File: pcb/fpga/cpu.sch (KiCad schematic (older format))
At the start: 53 parts, among them CON1 USB-MINI-B, P1 BANK1, P2 BANK2, P3 CONN_6, P4 BANK3, P5 BANK4, P6 PWR, U1 EPCS1, U2 EP1C3T100, U3 BA15BC0FP-E2_-_LDO, U4 LM1084IS-3.3/NOPB

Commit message: Latest pcb
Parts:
- removed C13, C6: 0.01uF, symbol Csmall
- removed U3: BA15BC0FP-E2_-_LDO, TO-252, symbol BA15BC0FP-E2_-_LDO
- added U2: LMS1585/7, TO-263, symbol LMS1585/7
- C1, C14, C15, C16, C17, C18: footprint (none) -> Capacitors_SMD:C_0805_HandSoldering
- C10: renamed from C7; footprint (none) -> Capacitors_SMD:C_0805_HandSoldering
- C11: renamed from C8; footprint (none) -> Capacitors_SMD:C_0805_HandSoldering
- C12: renamed from C9; footprint (none) -> Capacitors_SMD:C_0805_HandSoldering
- C13: renamed from C11; footprint (none) -> Capacitors_SMD:C_0805_HandSoldering
- C19: renamed from C23; footprint (none) -> Capacitors_SMD:c_elec_4x5.3
- C2: renamed from C3; footprint (none) -> Capacitors_SMD:C_0805_HandSoldering
- C20: renamed from C25; footprint (none) -> Capacitors_SMD:c_elec_4x5.3
- C21: renamed from C27; footprint (none) -> Capacitors_SMD:c_elec_4x5.3
- C22: renamed from C19; footprint (none) -> Capacitors_SMD:c_elec_4x5.3
- C23: renamed from C20; footprint (none) -> Capacitors_SMD:C_0805
- C24: renamed from C21; footprint (none) -> Capacitors_SMD:C_0805
- C25: renamed from C2; footprint (none) -> Capacitors_SMD:C_0805
- C3: renamed from C5; footprint (none) -> Capacitors_SMD:C_0805_HandSoldering
- C4: renamed from C10; footprint (none) -> Capacitors_SMD:C_0805_HandSoldering
- C5: renamed from C12; footprint (none) -> Capacitors_SMD:C_0805_HandSoldering
- C6: renamed from C22; footprint (none) -> Capacitors_SMD:c_elec_4x4.5
- C7: renamed from C24; footprint (none) -> Capacitors_SMD:c_elec_4x4.5
- C8: renamed from C26; footprint (none) -> Capacitors_SMD:c_elec_4x4.5
- C9: renamed from C4; footprint (none) -> Capacitors_SMD:C_0805_HandSoldering
- CON1: footprint (none) -> Connect:USB_Mini-B
- D1, D2, D3, D4, D5, D6, D7, D8: footprint (none) -> LEDs:LED-0805
- FB1: renamed from FB2; footprint (none) -> Resistors_SMD:R_2816_HandSoldering
- FB2: renamed from FB1; footprint (none) -> Resistors_SMD:R_2816_HandSoldering
- OSC1: value 501AAA -> Si501AAA
- P1: renamed from P6; footprint (none) -> Pin_Headers:Pin_Header_Straight_1x02
- P2: renamed from P4; footprint (none) -> Pin_Headers:Pin_Header_Straight_2x08
- P3: renamed from P1; footprint (none) -> Pin_Headers:Pin_Header_Straight_2x06
- P4: renamed from P2; footprint (none) -> Pin_Headers:Pin_Header_Straight_2x09
- P5: footprint (none) -> Pin_Headers:Pin_Header_Straight_2x09
- P6: renamed from P3; footprint (none) -> Pin_Headers:Pin_Header_Straight_1x06
- R1: renamed from R2; footprint (none) -> Resistors_SMD:R_0805_HandSoldering
- R2: renamed from R1; footprint (none) -> Resistors_SMD:R_0805_HandSoldering
- RP1: footprint (none) -> Resistors_SMD:R_Array_Convex_4x1206
- RP2: footprint (none) -> Resistors_SMD:R_Array_Convex_8x0602
- U1: footprint (none) -> SMD_Packages:SOIC-8-N
- U3: renamed from U4; footprint TO-263 -> SMD_Packages:TO-263
- U4: renamed from U2; footprint (none) -> Housings_QFP:TQFP-100_14x14mm_Pitch0.5mm
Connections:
- net +1.5V: now also U2.2 (OUT); no longer C1.1, C13.1, C14.1, C15.1, C16.1, C17.1, C18.1, C20.1, C21.1, C22.1, C23.1, C24.1, C25.1, C4.1, C5.1, FB2.2, OSC1.4 (VDD), P1.1 (P1), P6.6, RP1.1 (P1), RP1.2 (P2), RP1.3 (P3), RP1.4 (P4), U1.3 (Vcc), U1.7 (Vcc), U1.8 (Vcc), U3.2 (OUT), U4.18 (VCCIO1), U4.31 (VCCIO4), U4.46 (VCCIO4), U4.59 (VCCIO3), U4.80 (VCCIO2), U4.9 (VCCA_PLL1), U4.95 (VCCIO2)
- net GND: no longer C6.2, C7.2, C8.2
- net at C19.1, C6.1, FB1.2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: now also U2.3 (IN)
- net 3V3 renamed +3.3V
- net +3.3V: now also C1.1, C13.1, C14.1, C15.1, C16.1, C17.1, C18.1, C20.1, C21.1, C25.1, C4.1, C5.1, OSC1.4 (VDD), P1.1 (P1), P6.6, RP1.1 (P1), RP1.2 (P2), RP1.3 (P3), RP1.4 (P4), U1.3 (Vcc), U1.7 (Vcc), U1.8 (Vcc), U3.2 (OUT), U4.18 (VCCIO1), U4.31 (VCCIO4), U4.46 (VCCIO4), U4.59 (VCCIO3), U4.80 (VCCIO2), U4.95 (VCCIO2)
- new net: C6.2, C7.2, C8.2, U2.1 (GND)
- new net VPLL: C22.1, C23.1, C24.1, FB2.2, U4.9 (VCCA_PLL1)

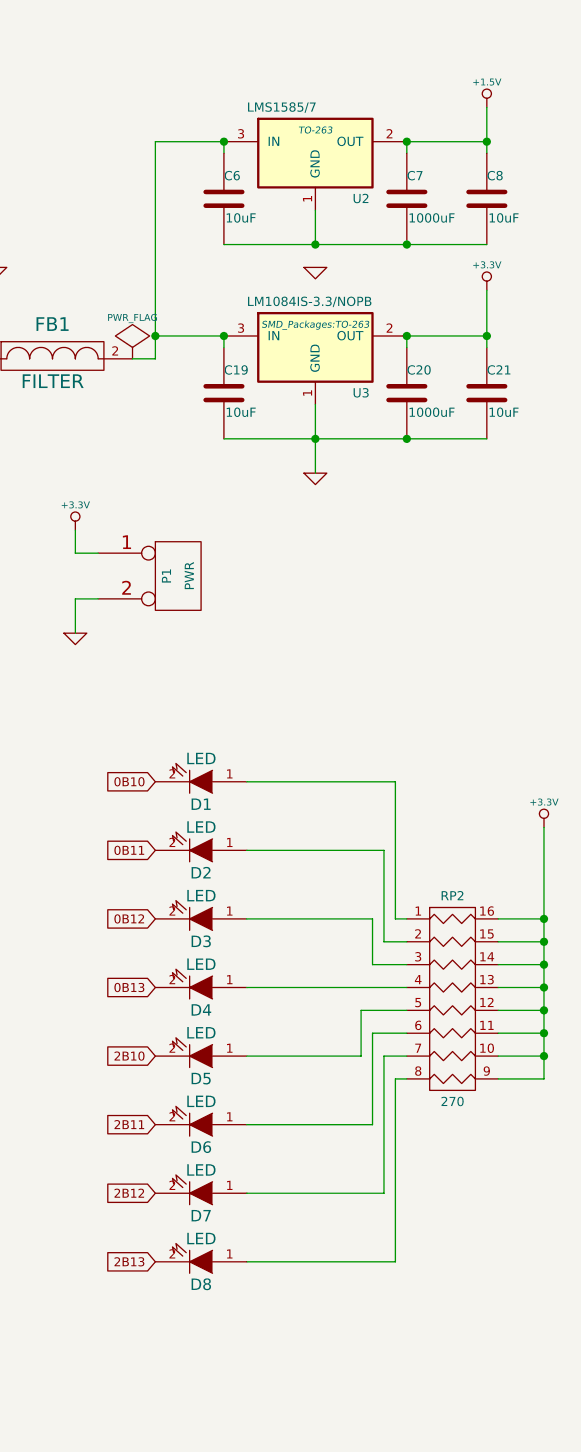
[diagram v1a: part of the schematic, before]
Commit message: Resistors replacing resistor network
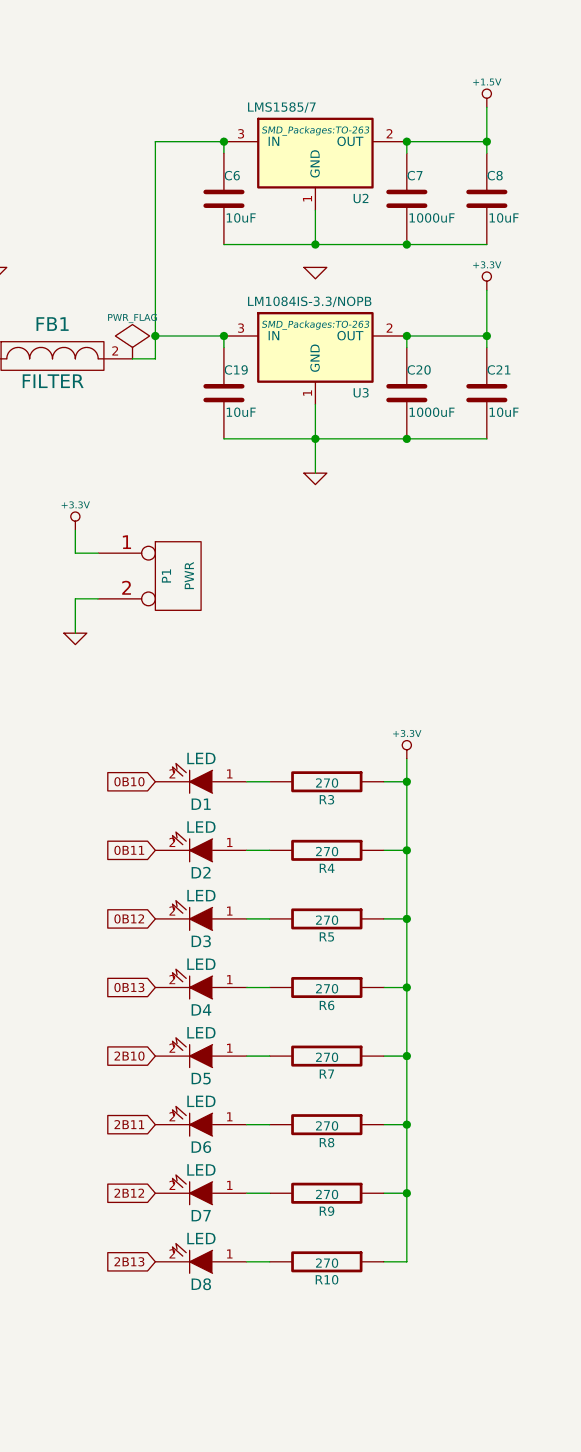
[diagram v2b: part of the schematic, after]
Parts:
- removed RP2: 270, Resistors_SMD:R_Array_Convex_8x0602, symbol R_PACK8
- added R10, R3, R4, R5, R6, R7, R8, R9: 270, Resistors_SMD:R_0805_HandSoldering, symbol R
- FB1, FB2: footprint Resistors_SMD:R_2816_HandSoldering -> Resistors_SMD:R_0805_HandSoldering
- OSC1: footprint (none) -> common-ICs:DFN4-Si501
- U2: footprint TO-263 -> SMD_Packages:TO-263
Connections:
- net +3.3V: now also R10.1, R3.1, R4.1, R5.1, R6.1, R7.1, R8.1, R9.1
- net at D3.1 (A): now also R5.2
- net at D1.1 (A): now also R3.2
- net at D2.1 (A): now also R4.2
- net at D4.1 (A): now also R6.2
- net at D5.1 (A): now also R7.2
- net at D6.1 (A): now also R8.2
- net at D7.1 (A): now also R9.2
- net at D8.1 (A): now also R10.2

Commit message: Modified schematic
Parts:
- removed U3: LM1084IS-3.3/NOPB, SMD_Packages:TO-263, symbol LM1084IS-3.3/NOPB
- added U3: LMS1585/7-3.3, SMD_Packages:TO-263, symbol LMS1585/7
- C1: Farnell (none) -> http://il.farnell.com/tdk/c2012x5r1a106m125ab/ceramic-capac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; PARTNO (none) -> C2012X5R1A106M125AB
- C10, C11, C12, C13, C14, C15, C16, C17, C18, C9: Farnell (none) -> http://il.farnell.com/multicomp/mc0805b224m250ct/ceramic-ca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; PARTNO (none) -> MC0805B224M250CT
- C19, C21, C22, C6, C8: Farnell (none) -> http://il.farnell.com/united-chemi-con/emve160ada100md55g/a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; PARTNO (none) -> EMVE160ADA100MD55G
- C2, C4: Farnell (none) -> http://il.farnell.com/murata/grm21br60j476me15l/cap-mlcc-x5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; PARTNO (none) -> GRM21BR60J476ME15L
- C20, C7: Farnell http://il.farnell.com/panasonic-electronic-components/eeefk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 -> http://il.farnell.com/wurth-elektronik/865080140004/cap-alu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; PARTNO EEEFK0J102AP -> 865080140004
- C23: Farnell (none) -> http://il.farnell.com/multicomp/mc0805b104m250ct/ceramic-ca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; PARTNO (none) -> MC0805B104M250CT
- C24: Farnell (none) -> http://il.farnell.com/multicomp/mc0805b102m500ct/ceramic-ca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; PARTNO (none) -> MC0805B102M500CT
- C25: Farnell (none) -> http://il.farnell.com/multicomp/mc0805f106z6r3ct/cap-mlcc-y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; PARTNO (none) -> MC0805F106Z6R3CT
- C3, C5: Farnell (none) -> http://il.farnell.com/multicomp/mc0805b104m160ct/ceramic-ca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; PARTNO (none) -> MC0805B104M160CT
- CON1: eBay (none) -> http://www.ebay.co.uk/itm/New-15-x-Mini-USB-B-5-Pin-Female-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
- D1: Farnell http://il.farnell.com/dialight/5988150107f/led-yellow-1-25m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 -> http://il.farnell.com/kingbright/kphcm-2012pbc-a/led-0805-b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; PARTNO 5988150107F -> KPHCM-2012PBC-A
- D2, D3, D4, D5, D6, D7, D8: Farnell (none) -> http://il.farnell.com/kingbright/kphcm-2012pbc-a/led-0805-b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; PARTNO (none) -> KPHCM-2012PBC-A
- FB1, FB2: Farnell http://il.farnell.com/tdk/mmz2012202bt000/ferrite-bead-0-5o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 -> http://il.farnell.com/tdk/mpz2012s300at000/ferrite-bead-0-0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; PARTNO MMZ2012Y202BT000 -> MPZ2012S300AT000
- P1, P6: eBay (none) -> http://www.ebay.co.uk/itm/New-40-Pin-2-54mm-Male-Female-SIL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
- P2, P3, P4, P5: eBay (none) -> http://www.ebay.co.uk/itm/3pcs-2-54mm-2-x-40-Pin-Male-Doubl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
- R1: Farnell (none) -> http://il.farnell.com/vishay-dale/crcw08052m21fkea/thick-fi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; PARTNO (none) -> CRCW08052M21FKEA
- R10, R3, R4, R5, R6, R7, R8, R9: Farnell (none) -> http://il.farnell.com/koa-spear-electronics/rn73h2attd2700b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; PARTNO (none) -> MC0805S8F2700T5E
- R2: Farnell (none) -> http://il.farnell.com/panasonic-electronic-components/erj-6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; PARTNO (none) -> ERJ-6GEYJ150V
- RP1: Farnell http://il.farnell.com/yageo/yc164-jr-0710kl/resistor-iso-ar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 -> http://il.farnell.com/yageo/yc124-jr-0710kl/resistor-isolat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; PARTNO YC164-JR-0710KL -> YC124-JR-0710KL
- U1: Farnell (none) -> http://il.farnell.com/altera/epcs1si8n/ic-serial-config-mem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
- U2: value LMS1585/7 -> LMS1585/7-1.5; Farnell (none) -> http://il.farnell.com/texas-instruments/lms1585acs-1-5-nopb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; PARTNO (none) -> http://il.farnell.com/texas-instruments/lms1585acs-1-5-nopb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
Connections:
- net +3.3V: now also U3.2 (OUT)
- net GND: now also U3.1 (GND)
- net at C19.1, C6.1, FB1.2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: now also U3.3 (IN)
